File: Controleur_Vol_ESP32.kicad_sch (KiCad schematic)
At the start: 53 parts, among them J1 Conn_01x03, J10 Conn_01x03, J12 Conn_01x03, J13 Conn_01x03, J14 Conn_01x04, J15 Screw_Terminal_01x02, J2 Conn_01x03, J3 Conn_01x03, J4 Conn_01x03, J5 Conn_01x03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

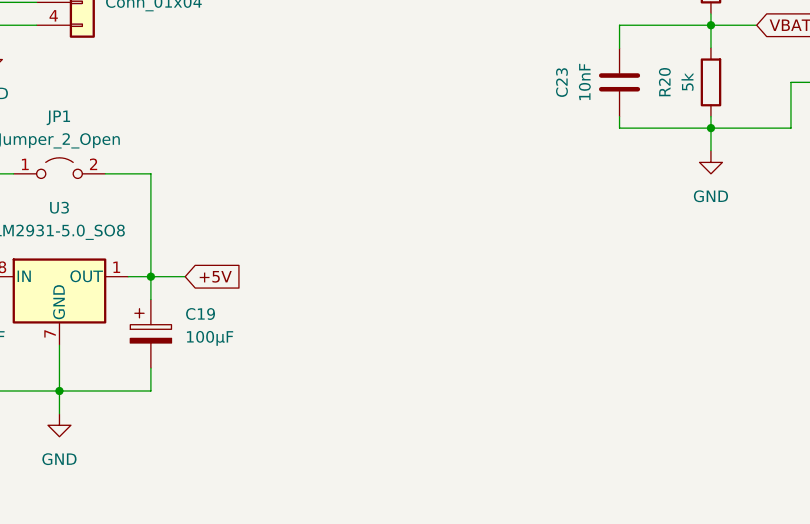
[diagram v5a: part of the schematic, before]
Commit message: Straps maillage massage + contour PCB
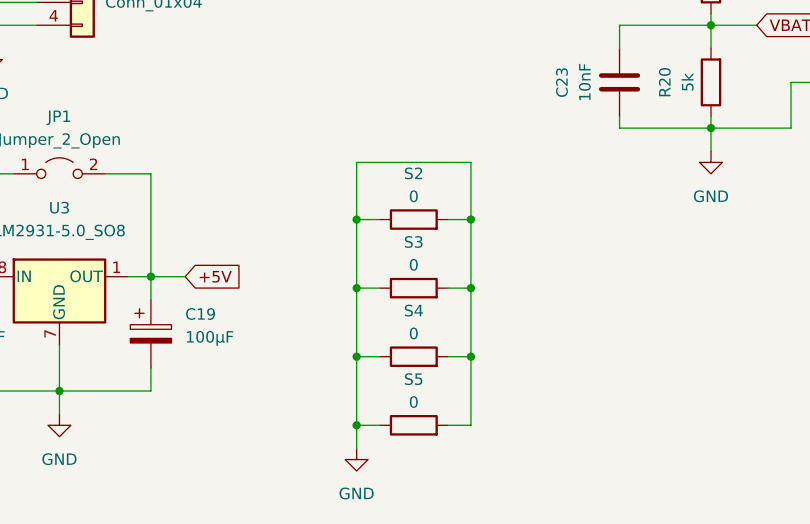
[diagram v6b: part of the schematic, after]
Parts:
- added S2, S3, S4, S5: 0, Resistor_SMD:R_1206_3216Metric_Pad1.30x1.75mm_HandSolder, symbol Device:R
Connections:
- net GND: now also S2.1, S2.2, S3.1, S3.2, S4.1, S4.2, S5.1, S5.2

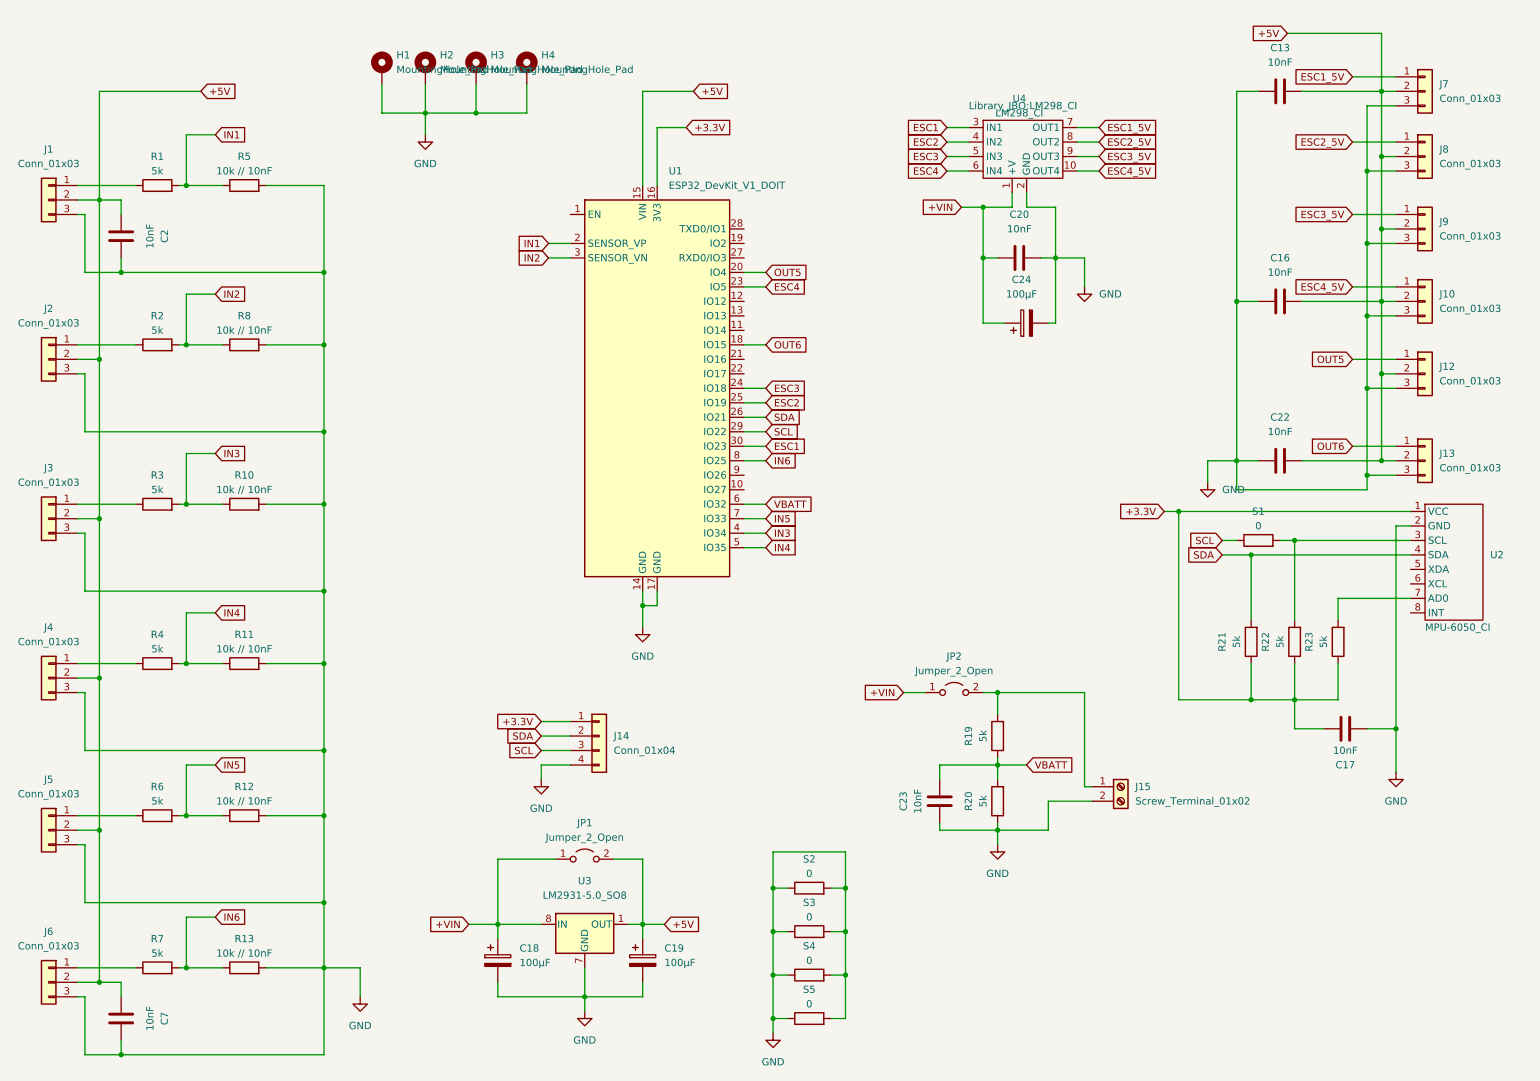
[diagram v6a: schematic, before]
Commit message: Ajout diodes "roue libre" sur sortie L293
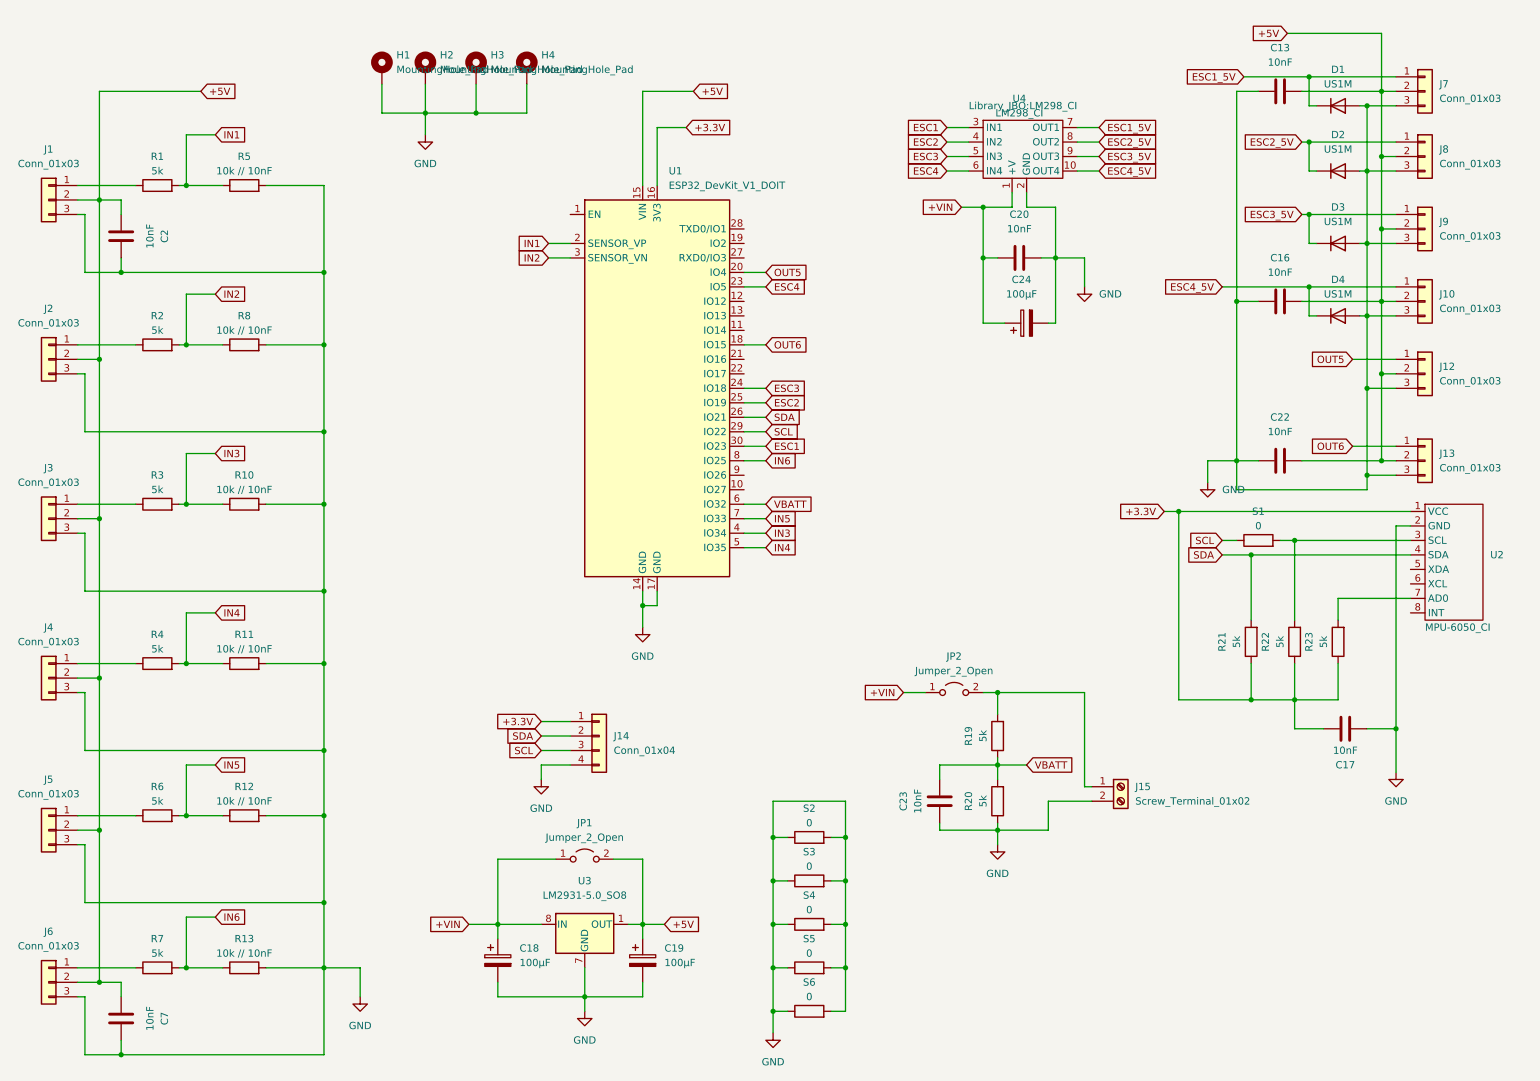
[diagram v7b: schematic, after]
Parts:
- added D1, D2, D3, D4: US1M, Diode_SMD:D_SMA, symbol Diode:US1M
- added S6: 0, Resistor_SMD:R_1206_3216Metric_Pad1.30x1.75mm_HandSolder, symbol Device:R
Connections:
- net ESC1_5V: now also D1.1 (K)
- net ESC2_5V: now also D2.1 (K)
- net ESC3_5V: now also D3.1 (K)
- net ESC4_5V: now also D4.1 (K)
- net GND: now also D1.2 (A), D2.2 (A), D3.2 (A), D4.2 (A), S6.1, S6.2
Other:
- moved on the sheet: S2, S3, S4, S5
